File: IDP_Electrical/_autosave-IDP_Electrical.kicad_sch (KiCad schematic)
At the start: 28 parts, among them M1 DC Motor Symbol, M2 DC Motor Symbol, U1 SER0038, U2 SER0038

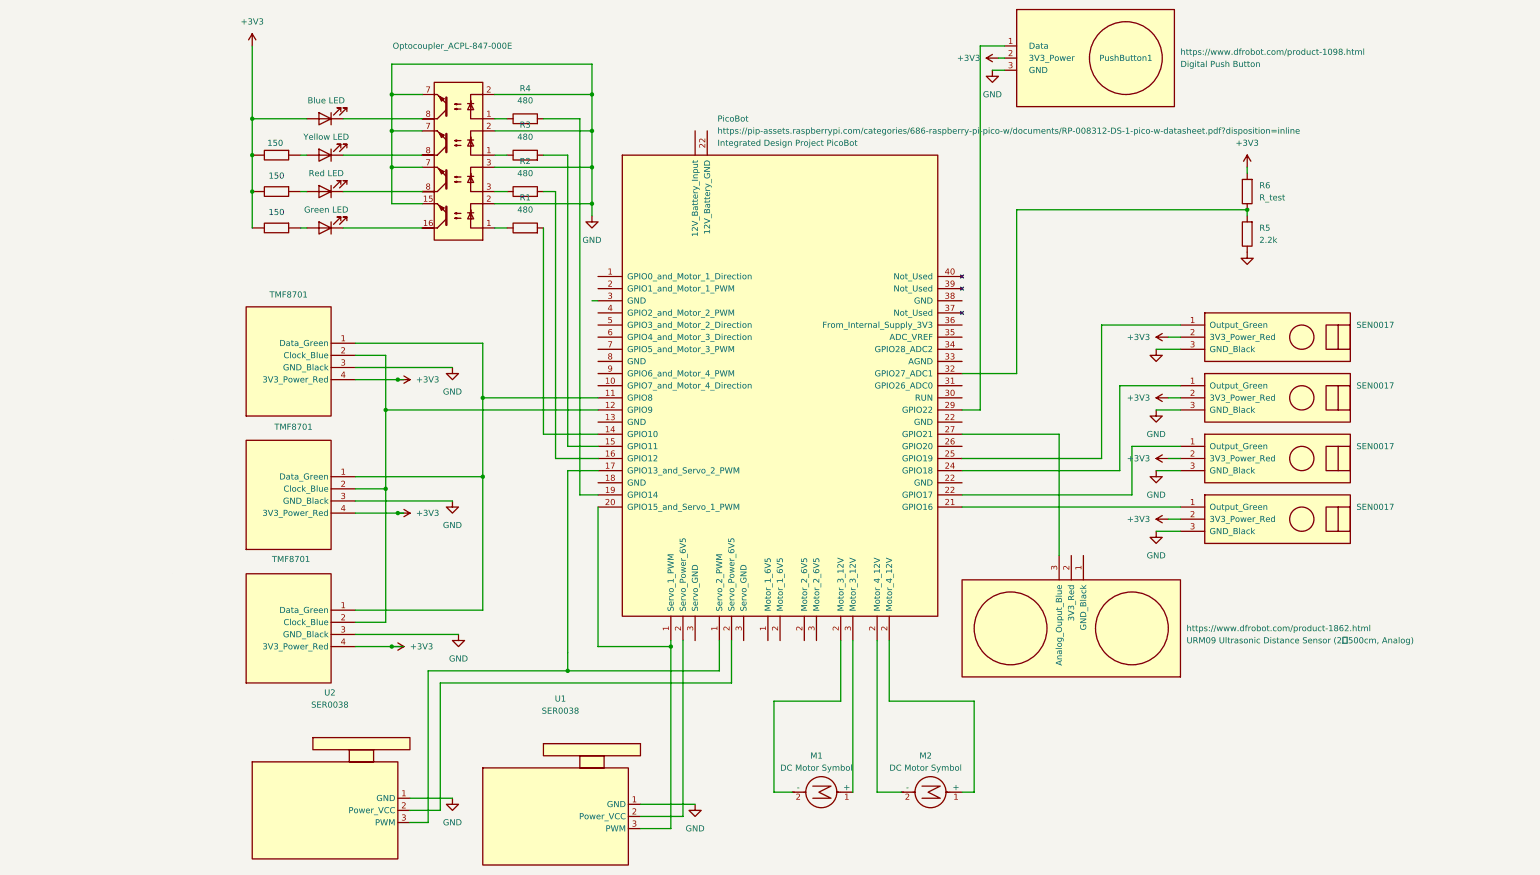
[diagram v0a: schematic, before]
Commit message: updated power and ground
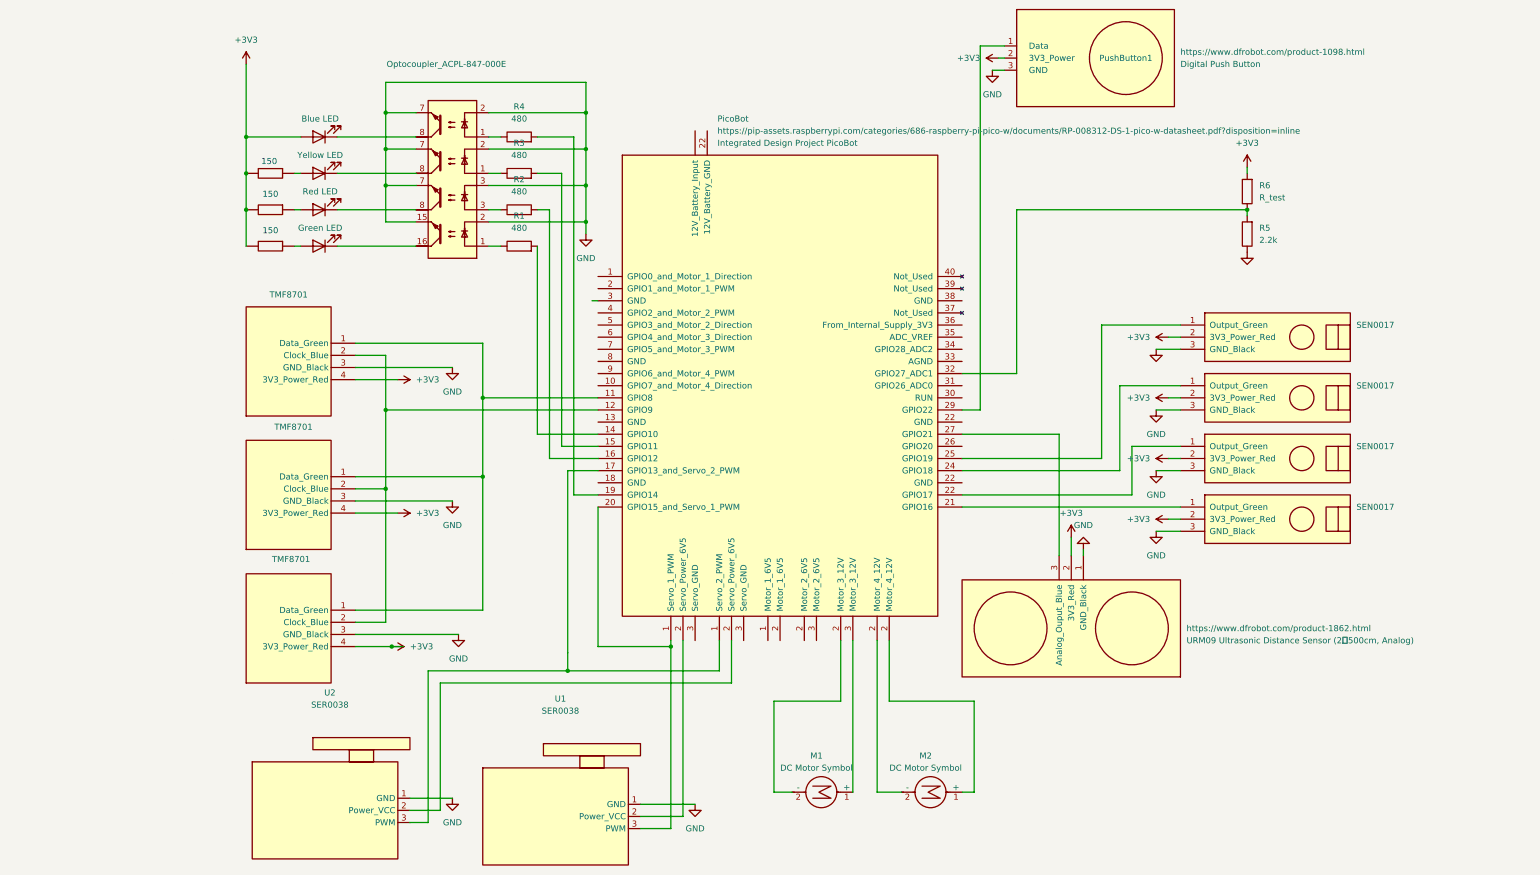
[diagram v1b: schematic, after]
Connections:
- net +3V3: now also SEN1.2 (3V3_Red)
- net GND: now also SEN1.1 (GND_Black)
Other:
- moved on the sheet: R1, R2, R3, R4
